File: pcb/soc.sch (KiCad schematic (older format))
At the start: 15 parts, among them IC5 CC2540F256RHAT, Y1 32 Mhz

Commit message: Replaced CC2540F256RHAT with CC2541F128RHAT
CC2540F256RHAT has a useless USB interface.
CC2541F128RHAT has better radio power consumption and reduced flash,
I don't need 256KB. Fingers crossed for some samples from TI.

EFR32 Blue Gecko was the best alternative so far but I opted for TI
because of its free CCS (versus IAR) environment. EFR32 has better
radio power consumption than TI chips but worse standby current
(1.4 vs 0.5 uA).
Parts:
- IC5: value CC2540F256RHAT -> CC2541F128RHAT; symbol CC2540F256RHAT -> CC2541F128RHAT; Description CC2540F256RHAT, System-On-Chip Microcontroller CMOS for Blu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 -> CC2541F128RHAT, System-On-Chip Microcontroller CMOS for Blu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; Manufacturer_Part_Number CC2540F256RHAT -> CC2541F128RHAT
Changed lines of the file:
@@
 LIBS:1N4148X-TP
 LIBS:TLV3691IDCKR
-LIBS:CC2540F256RHAT
+LIBS:CC2541F128RHAT
 LIBS:pir-cache
 EELAYER 25 0
@@
 PIR_LOW
 $Comp
-L CC2540F256RHAT IC5
+L CC2541F128RHAT IC5
 U 1 1 5A76B408
 P 3300 2850
 F 0 "IC5" H 4750 3900 50  0000 L CNN
-F 1 "CC2540F256RHAT" H 3750 3000 50  0000 L CNN
+F 1 "CC2541F128RHAT" H 3750 3000 50  0000 L CNN
 F 2 "QFN50P600X600X100-41N" H 4750 1200 50  0001 L CNN
 F 3 "http://www.ti.com/lit/ds/symlink/cc2540.pdf" H 4750 1100 50  0001 L CNN
-F 4 "CC2540F256RHAT, System-On-Chip Microcontroller CMOS for Bluetooth, 2 to 3.6V 40-Pin VQFN" H 4750 1000 50  0001 L CNN "Description"
+F 4 "CC2541F128RHAT, System-On-Chip Microcontroller CMOS for Bluetooth, 2 to 3.6V 40-Pin VQFN" H 4750 1000 50  0001 L CNN "Description"
 F 5 "RS" H 4750 900 50  0001 C CNN "Supplier_Name"
 F 6 "7300534P" H 4750 800 50  0001 C CNN "RS Part Number"
 F 7 "Texas Instruments" H 4750 700 50  0001 C CNN "Manufacturer_Name"
-F 8 "CC2540F256RHAT" H 4750 600 50  0001 C CNN "Manufacturer_Part_Number"
+F 8 "CC2541F128RHAT" H 4750 600 50  0001 C CNN "Manufacturer_Part_Number"
 F 9 "" H 4750 500 50  0001 C CNN "Allied_Number"
 F 10 "" H 4750 400 50  0001 C CNN "Other Part Number"

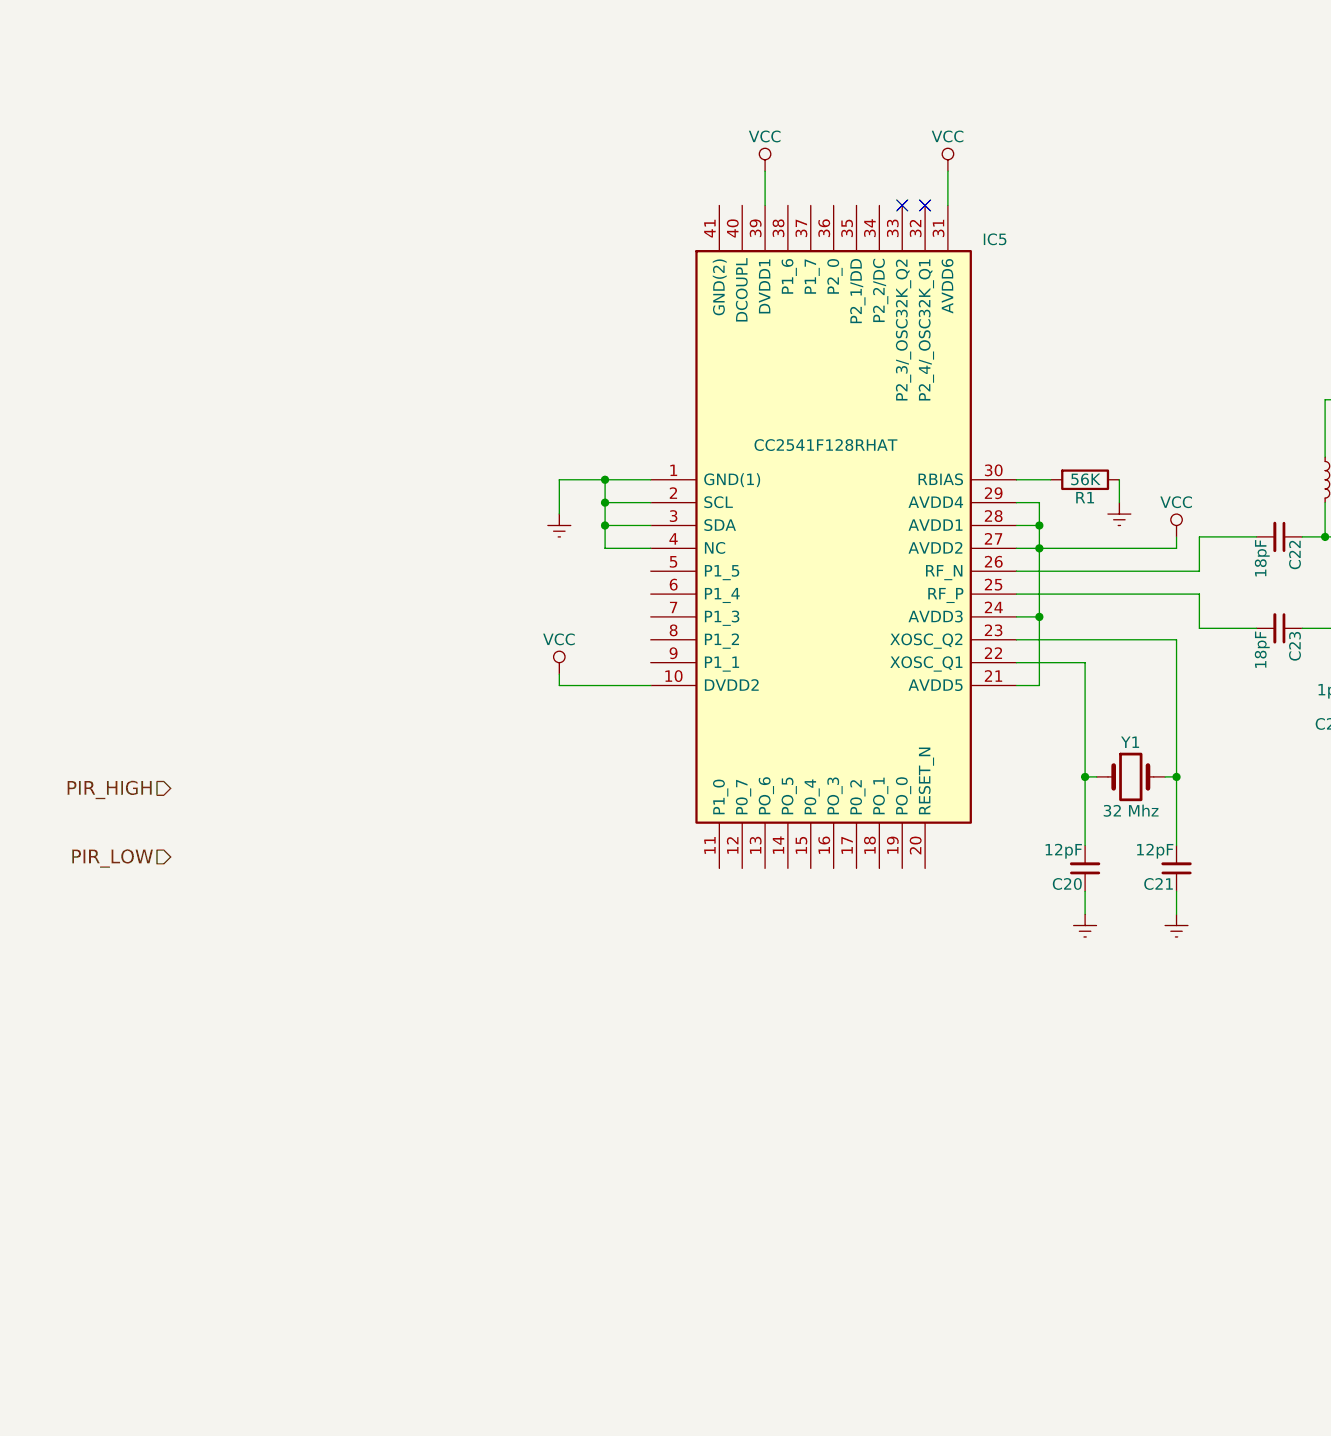
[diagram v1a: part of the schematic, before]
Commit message: Added debugger interface
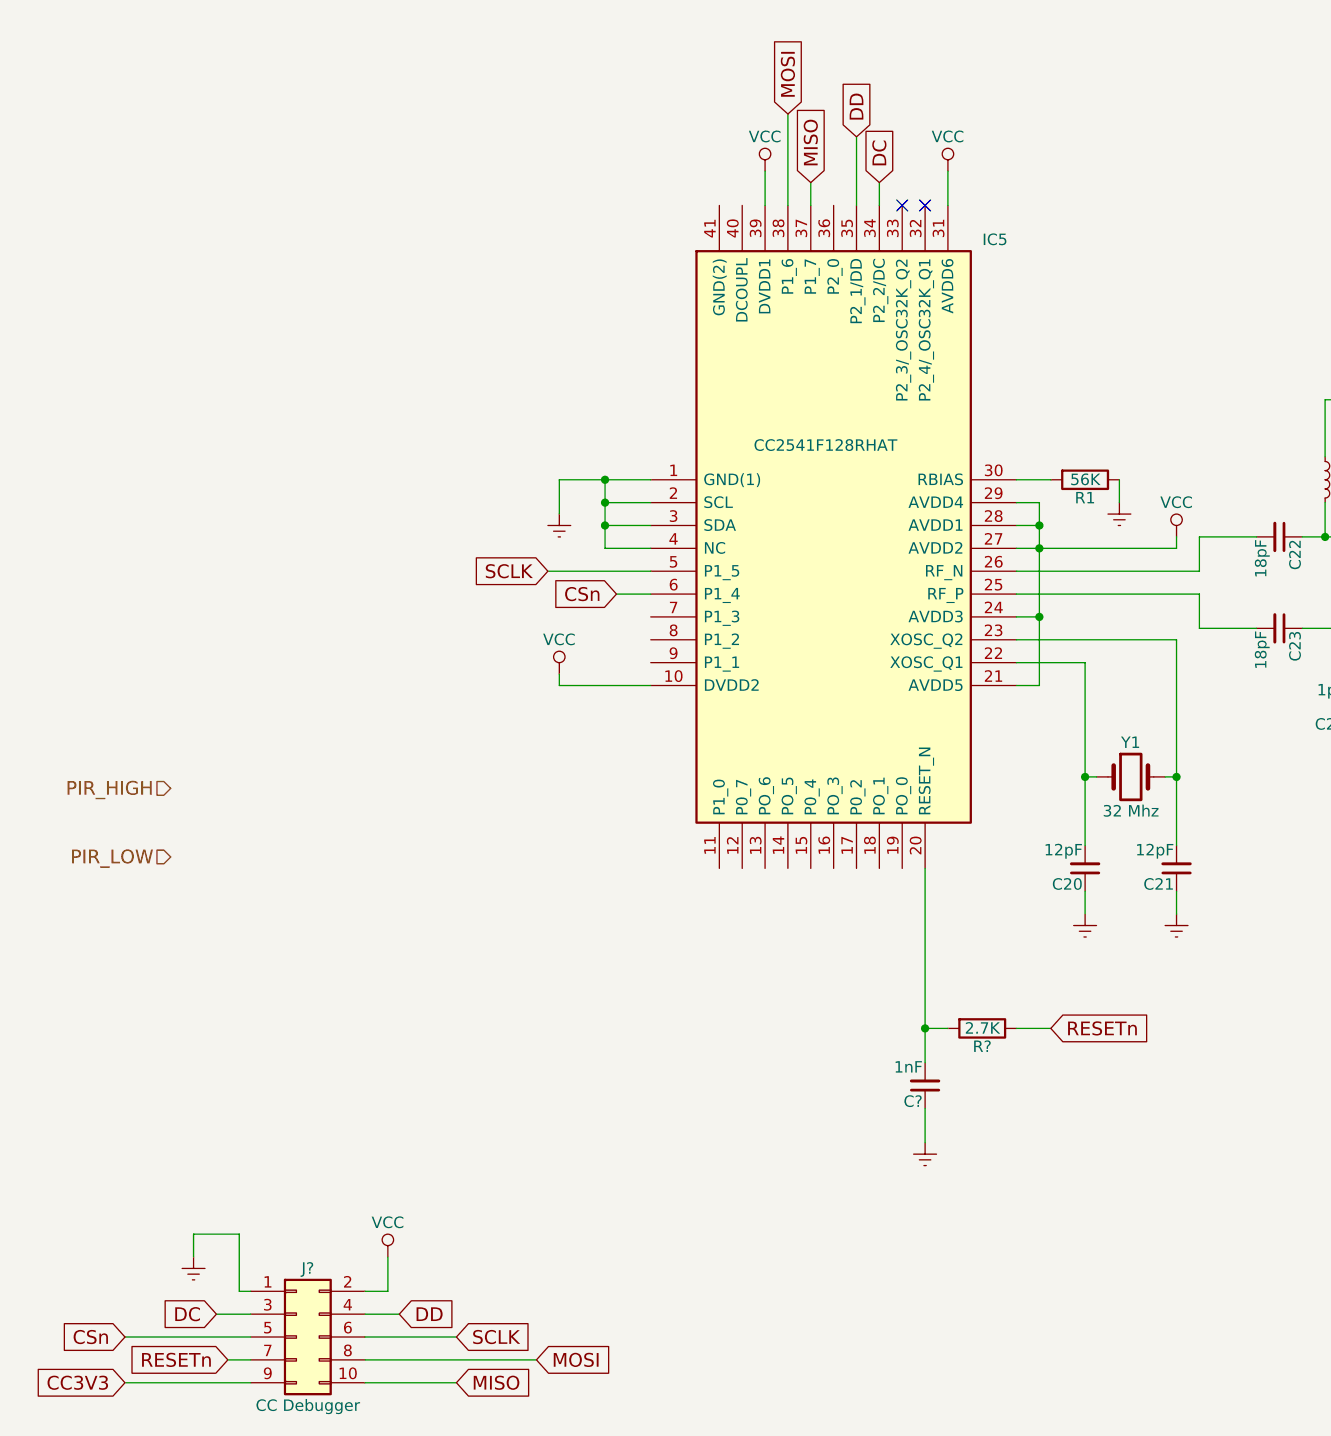
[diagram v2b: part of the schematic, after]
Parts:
- added C?: 1nF, symbol C_Small
- added J?: CC Debugger, symbol Conn_02x05_Odd_Even
- added R?: 2.7K, symbol R
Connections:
- net Earth: now also C?.1, J?.1 (Pin_1)
- net VCC: now also J?.2 (Pin_2)
- net at IC5.20 (RESET_N): now also C?.2, R?.2
- net DC: now reaches IC5.34 (P2_2/DC)
- net DC: now also J?.3 (Pin_3)
- net DD: now reaches IC5.35 (P2_1/DD)
- net DD: now also J?.4 (Pin_4)
- net MISO: now reaches IC5.37 (P1_7)
- net MISO: now also J?.10 (Pin_10)
- net MOSI: now reaches IC5.38 (P1_6)
- net MOSI: now also J?.8 (Pin_8)
- net SCLK: now reaches IC5.5 (P1_5)
- net SCLK: now also J?.6 (Pin_6)
- net CSn: now reaches IC5.6 (P1_4)
- net CSn: now also J?.5 (Pin_5)
- new net CC3V3: J?.9 (Pin_9)
- new net RESETn: J?.7 (Pin_7), R?.1
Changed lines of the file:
@@
 LIBS:contrib
 LIBS:valves
-LIBS:IRA-S210ST01
 LIBS:LPV802DGKT
 LIBS:SI2323DS-T1-E3
 LIBS:1N4148X-TP
 LIBS:TLV3691IDCKR
+LIBS:IRA-S210ST01
+LIBS:CC2540F256RHAT
+LIBS:CC2541F256RHAR
 LIBS:CC2541F128RHAT
 LIBS:pir-cache
@@
 Wire Wire Line
 	5600 4650 5600 4750
+Text GLabel 4200 1350 1    60   Input ~ 0
+DD
+Text GLabel 4300 1550 1    60   Input ~ 0
+DC
+Wire Wire Line
+	4300 1650 4300 1550
+Wire Wire Line
+	4200 1650 4200 1350
+$Comp
+L Conn_02x05_Odd_Even J?
+U 1 1 5A762773
+P 1750 6600
+F 0 "J?" H 1800 6900 50  0000 C CNN
+F 1 "CC Debugger" H 1800 6300 50  0000 C CNN
+F 2 "" H 1750 6600 50  0001 C CNN
+F 3 "" H 1750 6600 50  0001 C CNN
+	1    1750 6600
+	1    0    0    -1
+$EndComp
+Text GLabel 1400 6500 0    60   Input ~ 0
+DC
+Text GLabel 2200 6500 2    60   Input ~ 0
+DD
+Wire Wire Line
+	2050 6500 2200 6500
+Wire Wire Line
+	1400 6500 1550 6500
+$Comp
+L Earth #PWR?
+U 1 1 5A762D06
+P 1300 6250
+F 0 "#PWR?" H 1300 6000 50  0001 C CNN
+F 1 "Earth" H 1300 6100 50  0001 C CNN
+F 2 "" H 1300 6250 50  0001 C CNN
+F 3 "" H 1300 6250 50  0001 C CNN
+	1    1300 6250
+	1    0    0    -1
+$EndComp
+Wire Wire Line
+	1550 6400 1500 6400
+Wire Wire Line
+	1500 6400 1500 6150
+Wire Wire Line
+	1500 6150 1300 6150
+Wire Wire Line
+	1300 6150 1300 6250
+$Comp
+L VCC #PWR?
+U 1 1 5A762F97
+P 2150 6250
+F 0 "#PWR?" H 2150 6100 50  0001 C CNN
+F 1 "VCC" H 2150 6400 50  0000 C CNN
+F 2 "" H 2150 6250 50  0001 C CNN
+F 3 "" H 2150 6250 50  0001 C CNN
+	1    2150 6250
+	1    0    0    -1
+$EndComp
+Wire Wire Line
+	2050 6400 2150 6400
+Wire Wire Line
+	2150 6400 2150 6250
+Text GLabel 1000 6600 0    60   Input ~ 0
+CSn
+Text GLabel 2450 6600 2    60   Input ~ 0
+SCLK
+Text GLabel 2800 6700 2    60   Input ~ 0
+MOSI
+Text GLabel 2450 6800 2    60   Input ~ 0
+MISO
+Wire Wire Line
+	1000 6600 1550 6600
+Wire Wire Line
+	2050 6600 2450 6600
+Wire Wire Line
+	2050 6700 2800 6700
+Wire Wire Line
+	2050 6800 2450 6800
+Text GLabel 1450 6700 0    60   Input ~ 0
+RESETn
+Wire Wire Line
+	1550 6700 1450 6700
+Text GLabel 1000 6800 0    60   Input ~ 0
+CC3V3
+Wire Wire Line
+	1550 6800 1000 6800
+Text GLabel 3150 3350 0    60   Input ~ 0
+CSn
+Text GLabel 2850 3250 0    60   Input ~ 0
+SCLK
+Wire Wire Line
+	3150 3350 3300 3350
+Wire Wire Line
+	3300 3250 2850 3250
+Text GLabel 3900 1250 1    60   Input ~ 0
+MOSI
+Text GLabel 4000 1550 1    60   Input ~ 0
+MISO
+Wire Wire Line
+	3900 1650 3900 1250
+Wire Wire Line
+	4000 1550 4000 1650
+$Comp
+L R R?
+U 1 1 5A7649A0
+P 4750 5250
+F 0 "R?" V 4830 5250 50  0000 C CNN
+F 1 "2.7K" V 4750 5250 50  0000 C CNN
+F 2 "" V 4680 5250 50  0001 C CNN
+F 3 "" H 4750 5250 50  0001 C CNN
+	1    4750 5250
+	0    1    1    0
+$EndComp
+Wire Wire Line
+	4500 4550 4500 5400
+Wire Wire Line
+	4500 5250 4600 5250
+Text GLabel 5050 5250 2    60   Input ~ 0
+RESETn
+Wire Wire Line
+	5050 5250 4900 5250
+$Comp
+L C_Small C?
+U 1 1 5A764EFF
+P 4500 5500
+F 0 "C?" H 4510 5570 50  0000 L CNN
+F 1 "1nF" H 4510 5420 50  0000 L CNN
+F 2 "" H 4500 5500 50  0001 C CNN
+F 3 "" H 4500 5500 50  0001 C CNN
+	1    4500 5500
+	-1   0    0    1
+$EndComp
+$Comp
+L Earth #PWR?
+U 1 1 5A764F83
+P 4500 5750
+F 0 "#PWR?" H 4500 5500 50  0001 C CNN
+F 1 "Earth" H 4500 5600 50  0001 C CNN
+F 2 "" H 4500 5750 50  0001 C CNN
+F 3 "" H 4500 5750 50  0001 C CNN
+	1    4500 5750
+	1    0    0    -1
+$EndComp
+Connection ~ 4500 5250
+Wire Wire Line
+	4500 5600 4500 5750
 $EndSCHEMATC

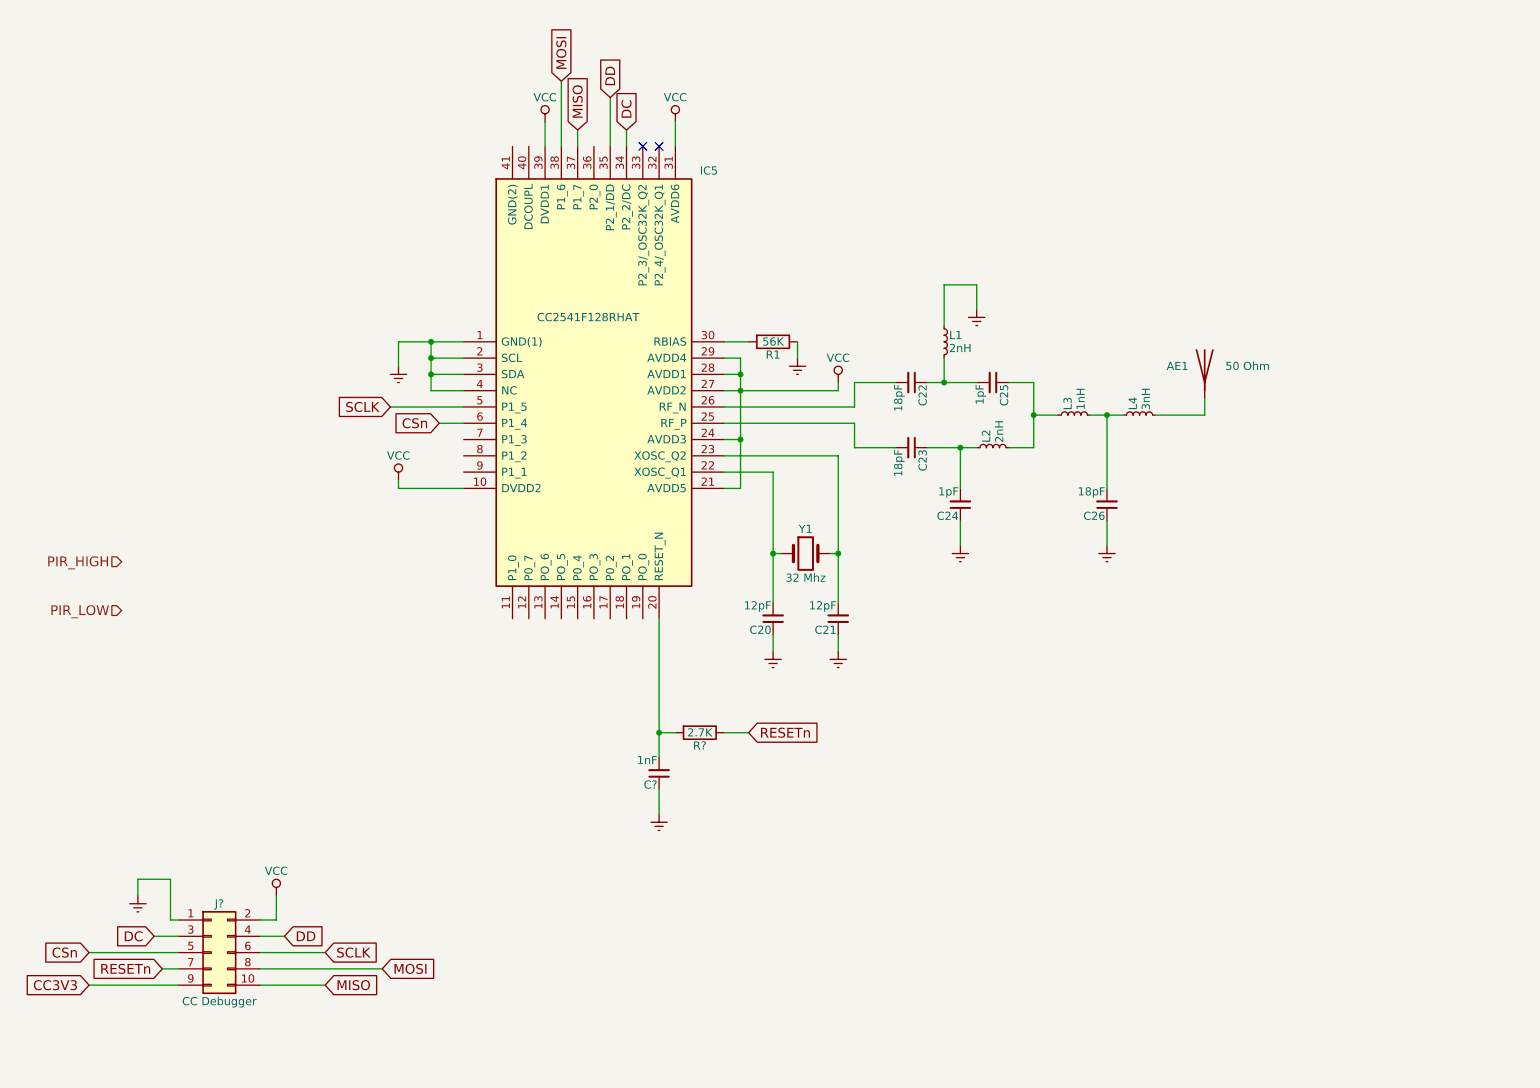
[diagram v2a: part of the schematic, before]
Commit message: User pushbutton
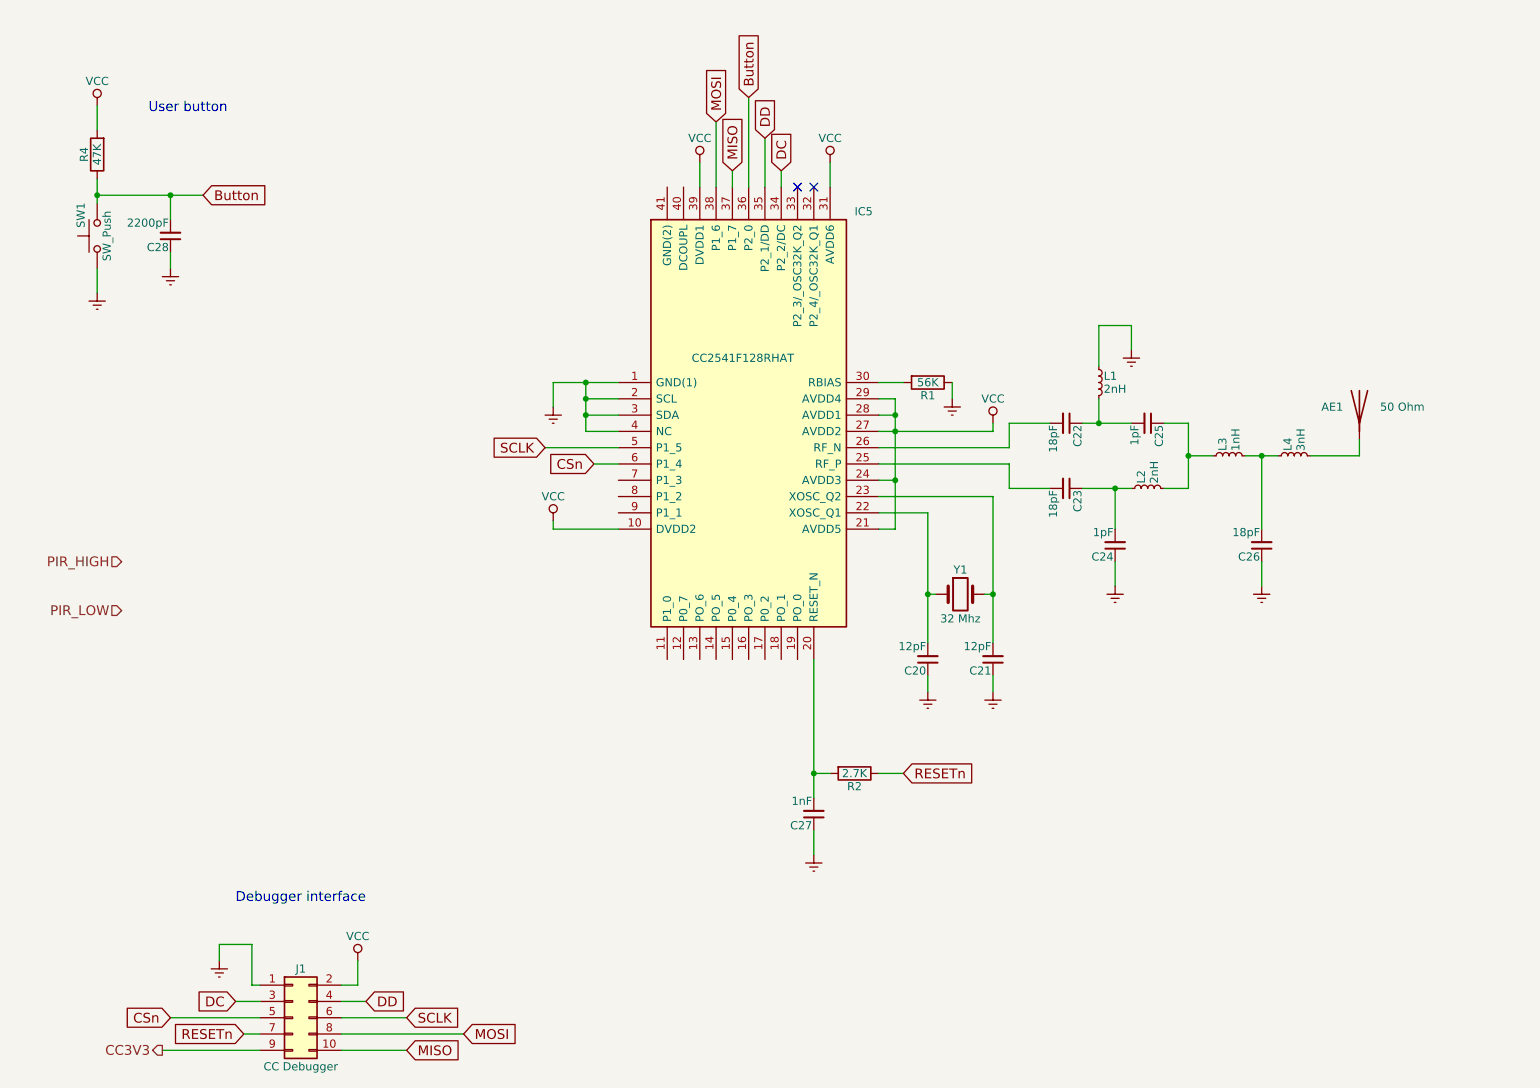
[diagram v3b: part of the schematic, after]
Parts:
- added C28: 2200pF, symbol C_Small
- added R4: 47K, symbol R
- added SW1: SW_Push, symbol SW_Push
- gave numbers to parts that had none: 3
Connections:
- net Earth: now also C28.1, SW1.1
- net VCC: now also R4.2
- net Button: now reaches IC5.36 (P2_0)
- net Button: now also C28.2, R4.1, SW1.2
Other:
- note added: "Debugger interface"
- note added: "User button"
- moved on the sheet: AE1, C20, C21, C22, C23, C24, C25, C26, C27, IC5, J1, L1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
